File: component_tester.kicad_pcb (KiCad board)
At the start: 2 copper layers, 70 x 48 mm, 91 parts, among them IC1 ATMEGA16U2, IC2 ATMEGA328P-A, P1 USB_OTG, P10 ICSP_prog_16u2_4, P11 BO_PC6, P12 ICSP_prog_16u2_5, P13 BO_PC5, P14 BO_PD2, P15 BO_PD3, P16 BO_PD4, P17 BO_PD5, P18 BO_PD6, P19 ICSP_prog_328_1, P2 BATTERY_CONNECTOR, P20 ICSP_prog_328_3, P21 ICSP_prog_328_4, P22 ICSP_prog_328_5, P23 CONN_01X01, P24 Device Under Test, P25 CONN_01X03, P3 Voltage_for_zener, P4 BO_PC7, P5 ICSP_prog_16u2_1, P6 BO_PD0, P7 BO_PD1, P8 BO_PC4, P9 ICSP_prog_16u2_3, Q1 TRANSISTOR_NPN_2N2222_KSP222A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, SW1 ON-OFF switch, SW2 DO_MEASUREMENT, SW3 CONNECT_CAP, U1 NCP1117ST50T3G, U2 XF2L-2625-1A, U3 LT1004, U4 CDSOT23-SRV05-4, U5 LP2985LV, Y1 8MHz, Y2 16MHz

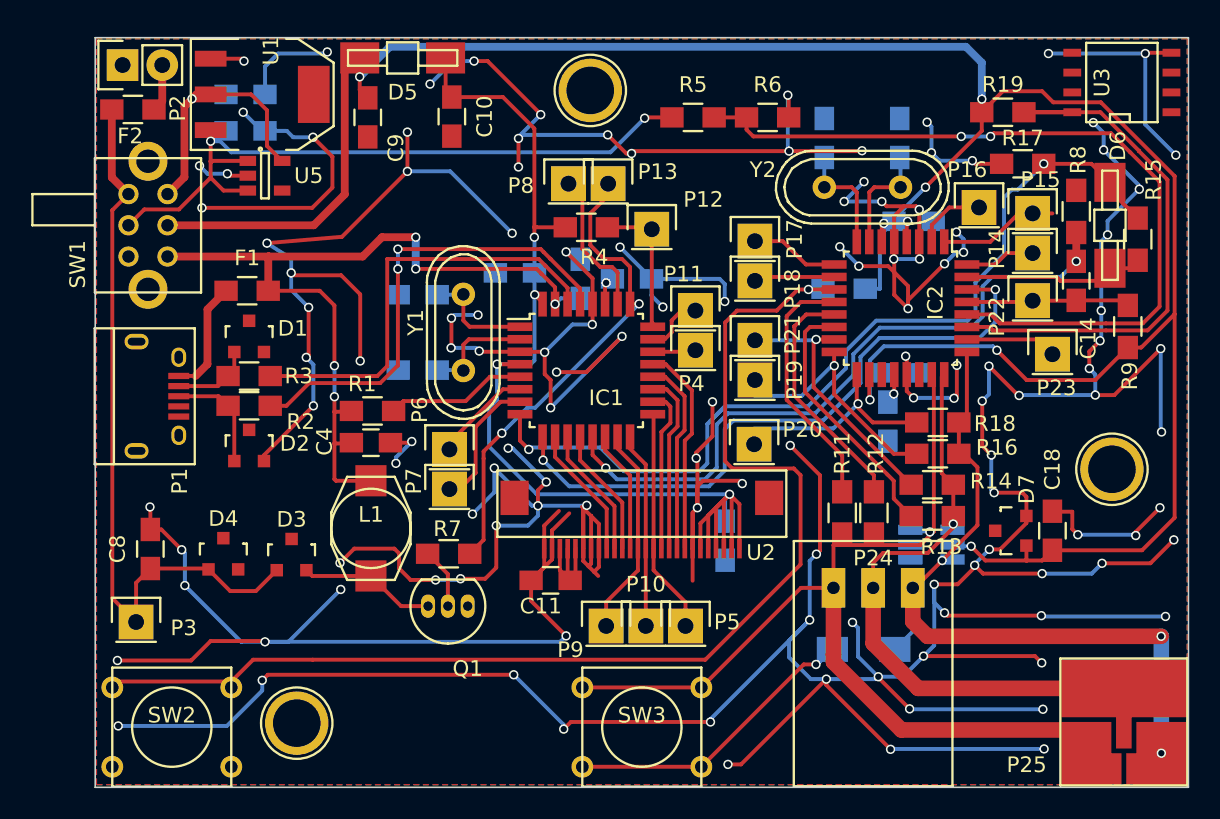
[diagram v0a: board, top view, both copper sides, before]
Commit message: Added the possibility of using a different LDO voltage regulator.
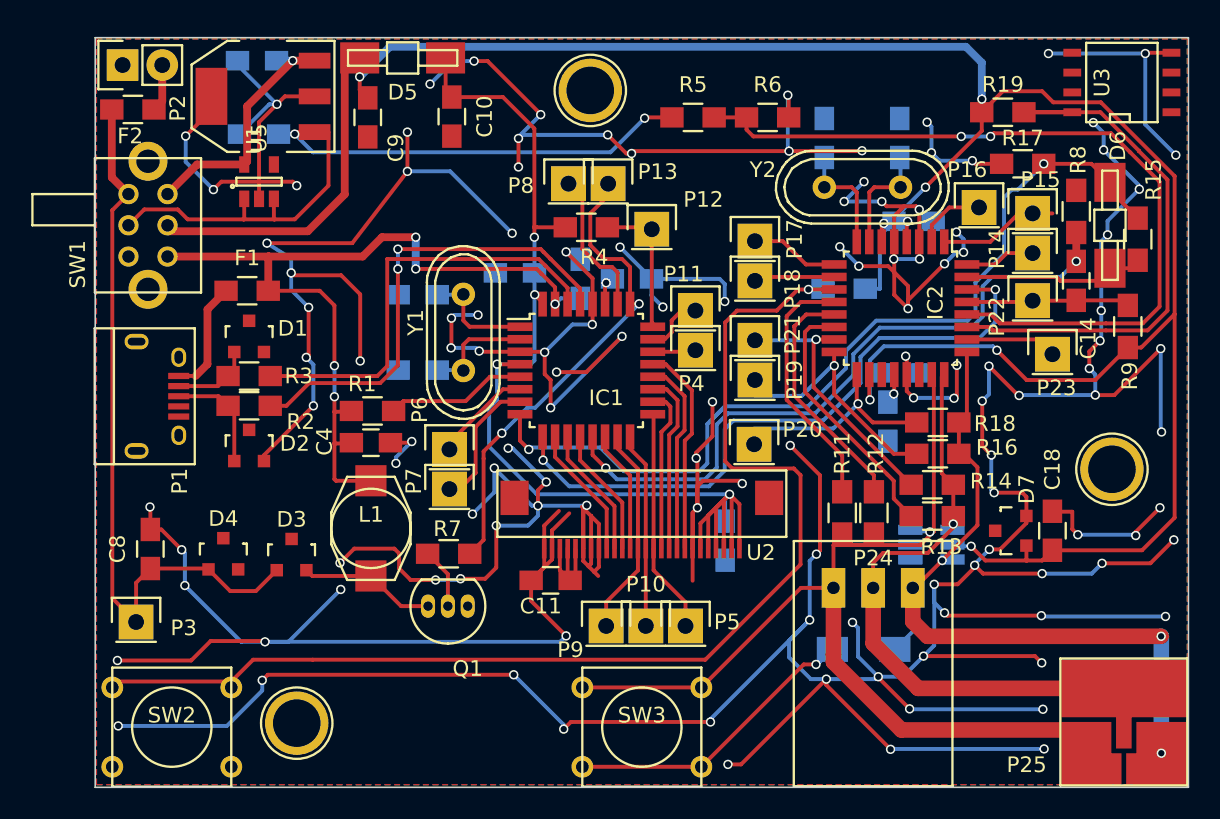
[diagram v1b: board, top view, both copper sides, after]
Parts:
- moved C7 2.28 mm to (110.4, 101.5), turned to 180 degrees
- moved C5 0.89 mm to (110.5, 106.2), turned to 180 degrees
- moved U5 0.54 mm to (110.5, 109.2), turned to 90 degrees
- moved U1 0.14 mm to (110.7, 103.8), turned to 90 degrees
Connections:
- U1 pad 1: GND -> Batt_Switch
- U1 pad 2: /Volt_reg_5v -> GND
- U1 pad 3: Batt_Switch -> /Volt_reg_5v
- U1 pad 4: (no net) -> GND
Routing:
- net /DUT1: track 65.8 -> 70.0 mm
- net Batt_Switch: track 46.8 -> 49.4 mm
- net /Volt_reg_5v: track 18.0 -> 16.1 mm
- net GND: vias 129 -> 126

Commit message: Moved USB port slightly further away from switch. As uploaded to DirtyPCBs
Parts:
- moved D2 2.29 mm to (109.9, 128.4), turned to 270 degrees
- moved P1 2.03 mm to (103.8, 125.0)
- moved R2 2.03 mm to (109.9, 125.6)
- moved R3 2.03 mm to (109.9, 123.7)
- moved D1 1.78 mm to (109.9, 120.9)
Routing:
- net GND: track 588.6 -> 592.5 mm
- net Net-(IC1-Pad29): track 30.4 -> 32.4 mm
- net Net-(F1-Pad1): track 7.35 -> 9.30 mm
- net /USB_D+: track 7.12 -> 5.97 mm
- net Net-(IC1-Pad30): track 28.0 -> 28.8 mm
